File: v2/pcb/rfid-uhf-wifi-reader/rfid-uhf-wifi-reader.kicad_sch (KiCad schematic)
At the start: 23 parts, among them J1 USB_OTG, J2 Conn_01x05, Q1 BSS138, Q2 BSS138, SW1 SW_Push, SW2 SW_Push, U1 ESP32-WROOM-32, U2 AMS1117-3.3, U3 CH340E

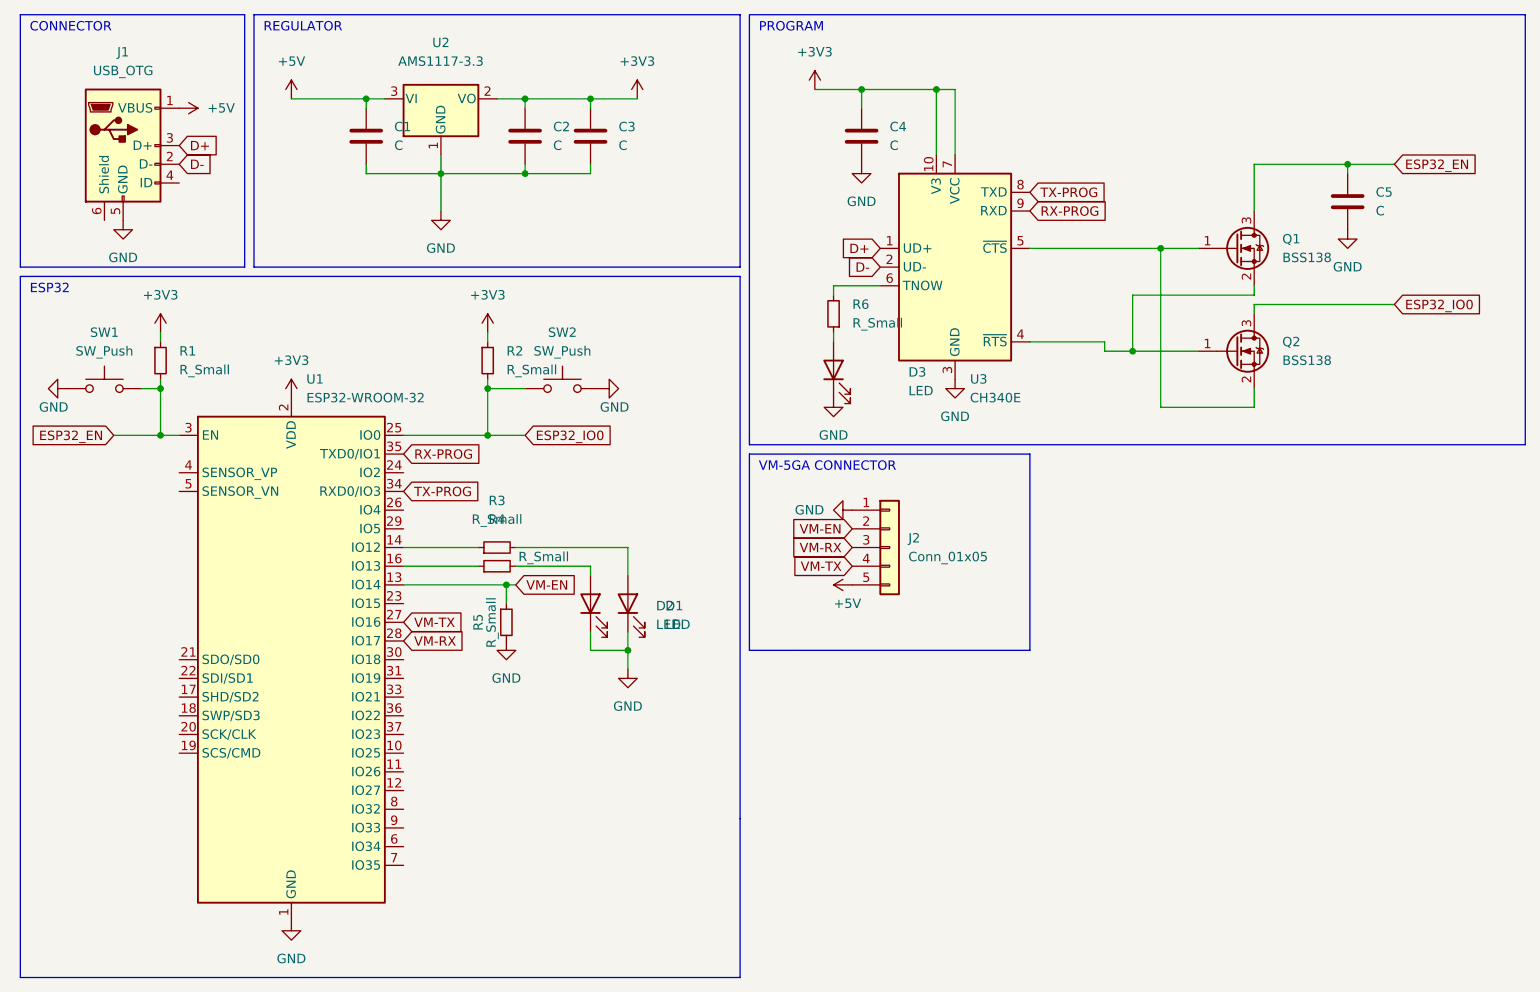
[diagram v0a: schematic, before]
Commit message: change ch340
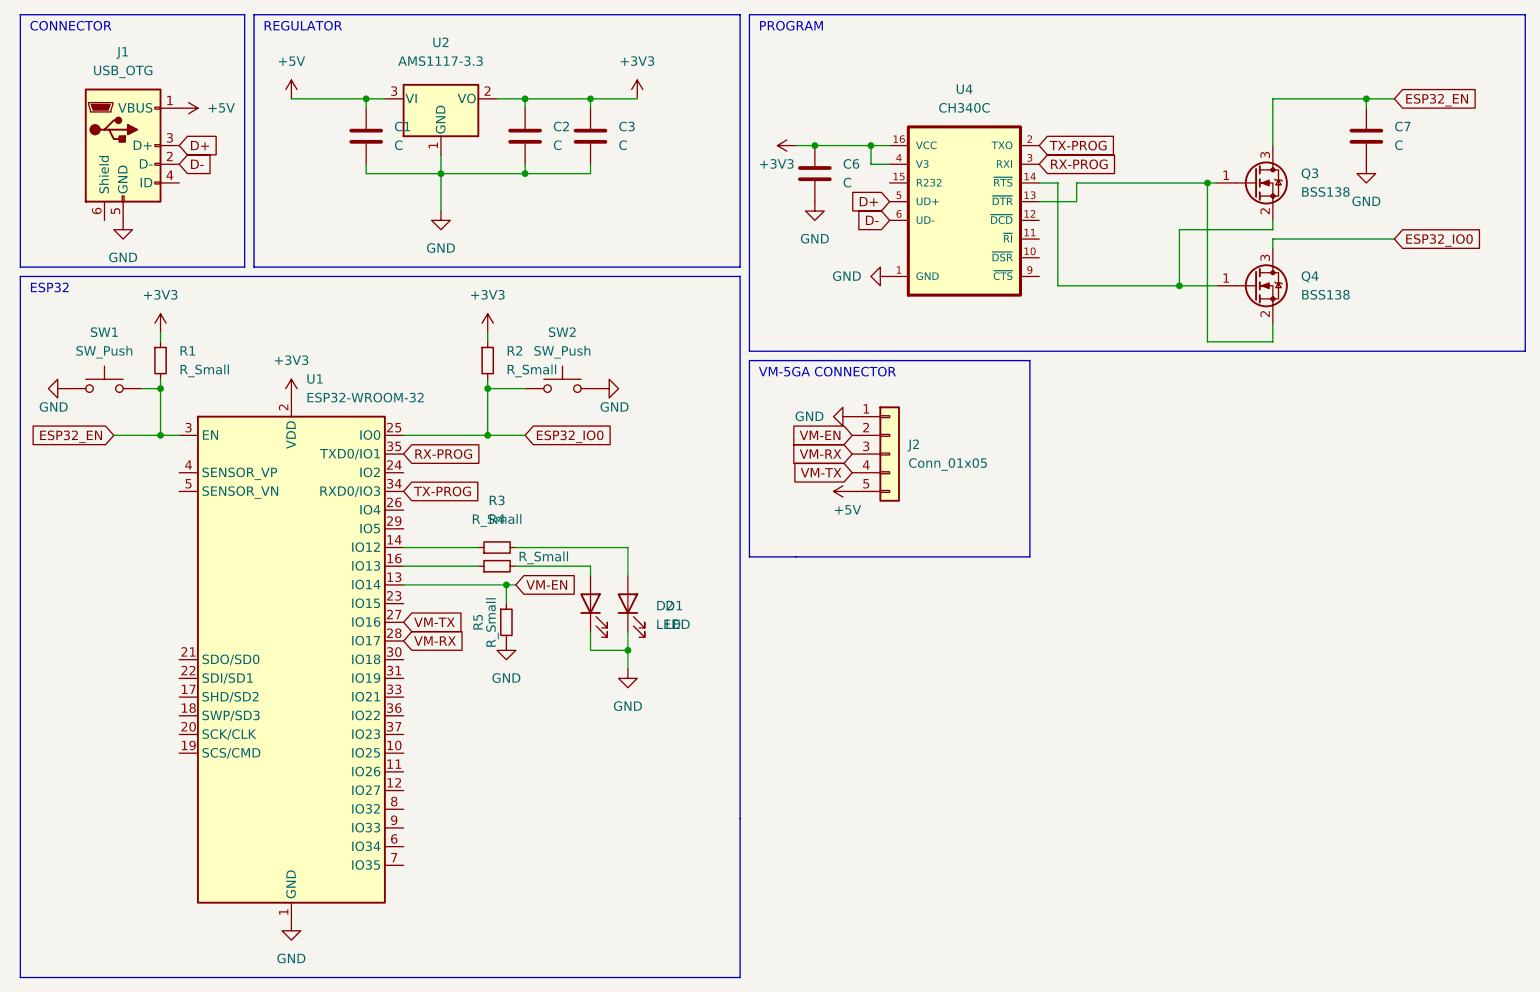
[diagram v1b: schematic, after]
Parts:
- removed C4, C5: C, Capacitor_SMD:C_0603_1608Metric, symbol Device:C
- removed D3: LED, LED_SMD:LED_0603_1608Metric, symbol Device:LED
- removed Q1, Q2: BSS138, Package_TO_SOT_SMD:SOT-23, symbol Transistor_FET:BSS138
- removed R6: R_Small, Resistor_SMD:R_0603_1608Metric, symbol Device:R_Small
- removed U3: CH340E, Package_SO:MSOP-10_3x3mm_P0.5mm, symbol Interface_USB:CH340E
- added C6, C7: C, Capacitor_SMD:C_0603_1608Metric, symbol Device:C
- added Q3, Q4: BSS138, Package_TO_SOT_SMD:SOT-23, symbol Transistor_FET:BSS138
- added U4: CH340C, CH340C:SO016, symbol CH340C:CH340C
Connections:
- net +3V3: now also C6.1, U4.16 (VCC), U4.4 (V3)
- net D+: now also U4.5 (UD+)
- net D-: now also U4.6 (UD-)
- net ESP32_EN: now also C7.1, Q3.3 (D)
- net ESP32_IO0: now also Q4.3 (D)
- net GND: now also C6.2, C7.2, U4.1 (GND)
- net RX-PROG: now also U4.3 (RXI)
- net TX-PROG: now also U4.2 (TXO)
- new net: Q3.2 (S), Q4.1 (G), U4.14 (~{RTS})
- new net: Q3.1 (G), Q4.2 (S), U4.13 (~{DTR})
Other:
- moved on the sheet: J2
